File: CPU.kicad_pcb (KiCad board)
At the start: 4 copper layers, 364 x 203 mm, 212 parts, among them J1 Conn_02x36_Top_Bottom, P10 Conn_02x08_Counter_Clockwise, P2 Conn_02x13_Top_Bottom, P3 Conn_02x13_Top_Bottom, P4 Conn_02x08_Counter_Clockwise, P5 Conn_02x25_Counter_Clockwise, P6 Conn_02x25_Counter_Clockwise, P7 Conn_02x07_Counter_Clockwise, P8 Conn_02x08_Counter_Clockwise

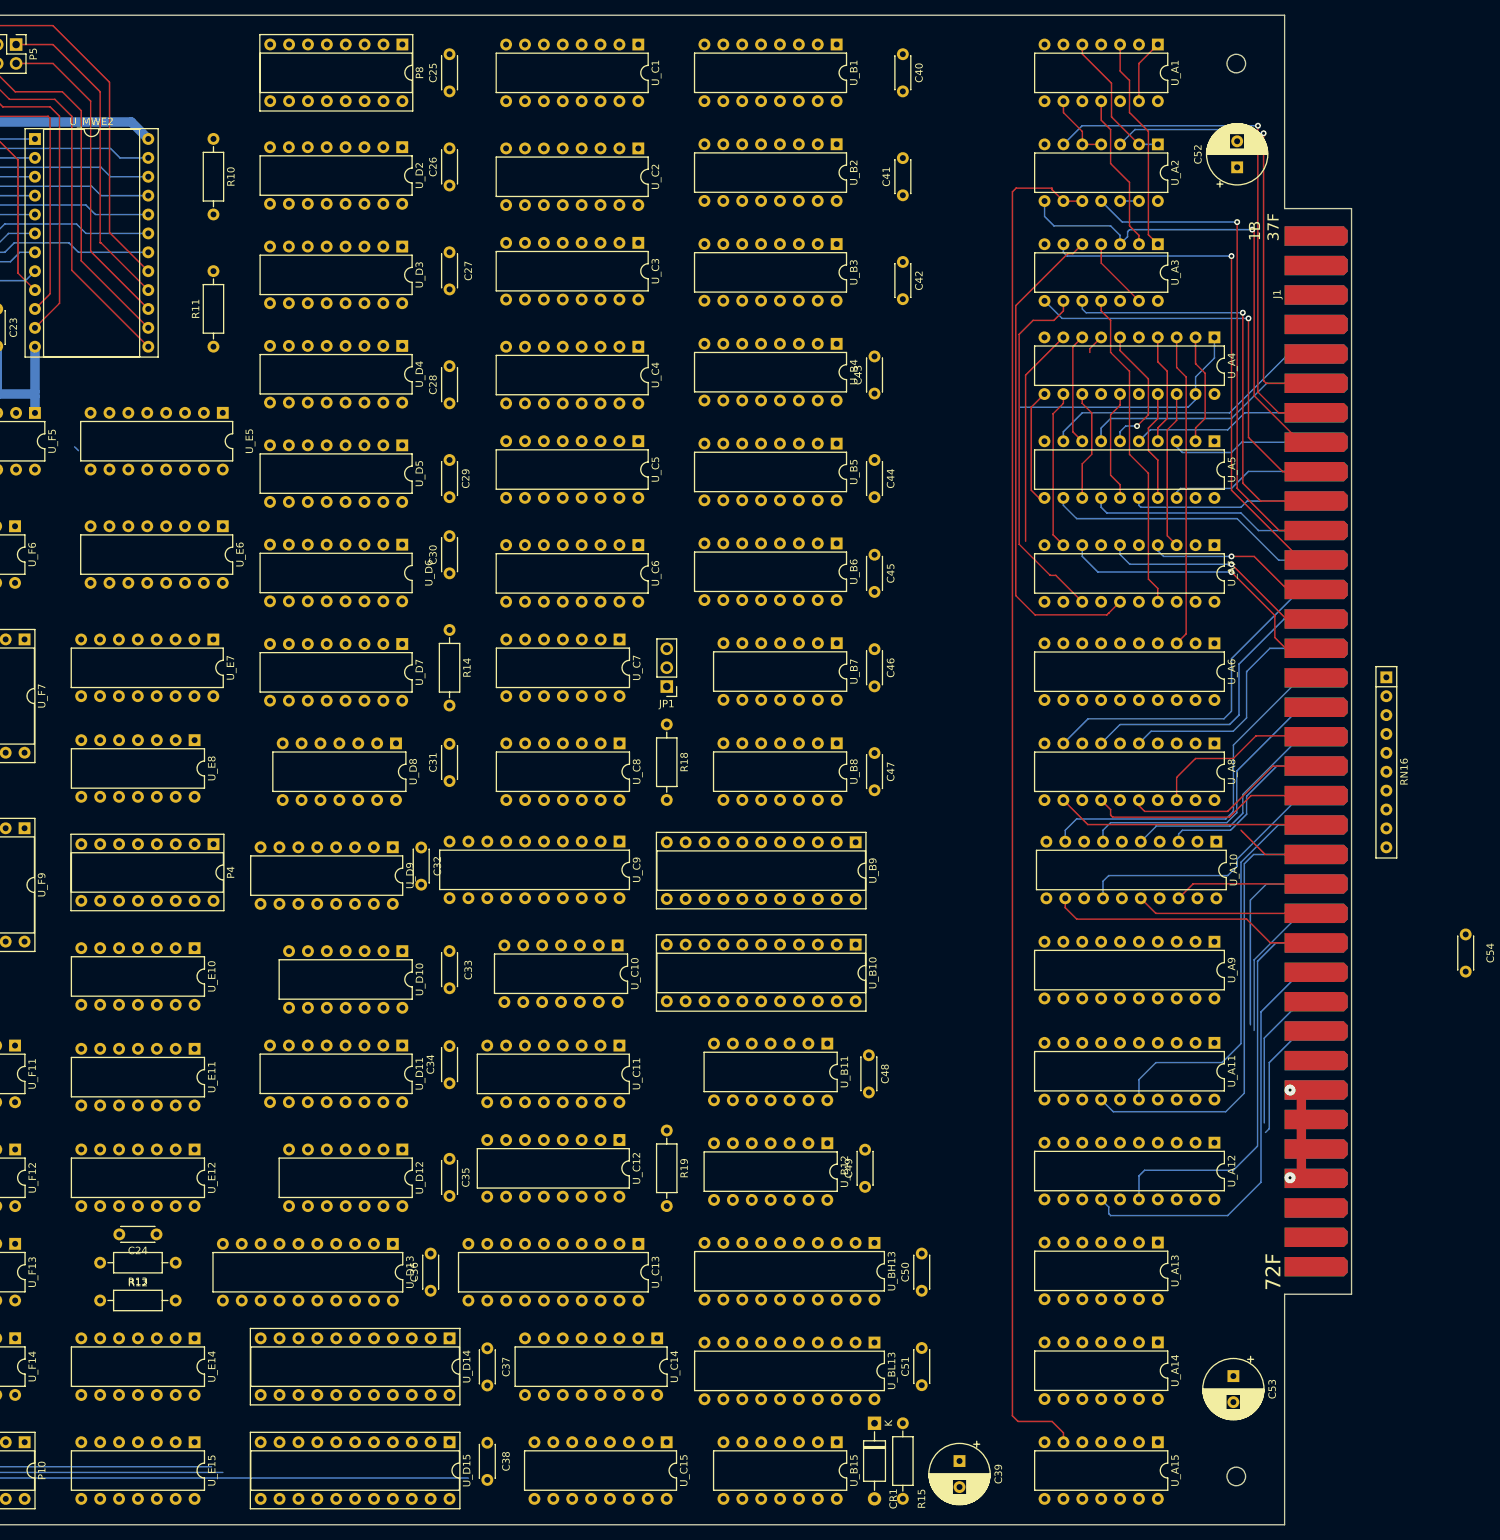
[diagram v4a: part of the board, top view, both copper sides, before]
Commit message: First row of chips successfully routed
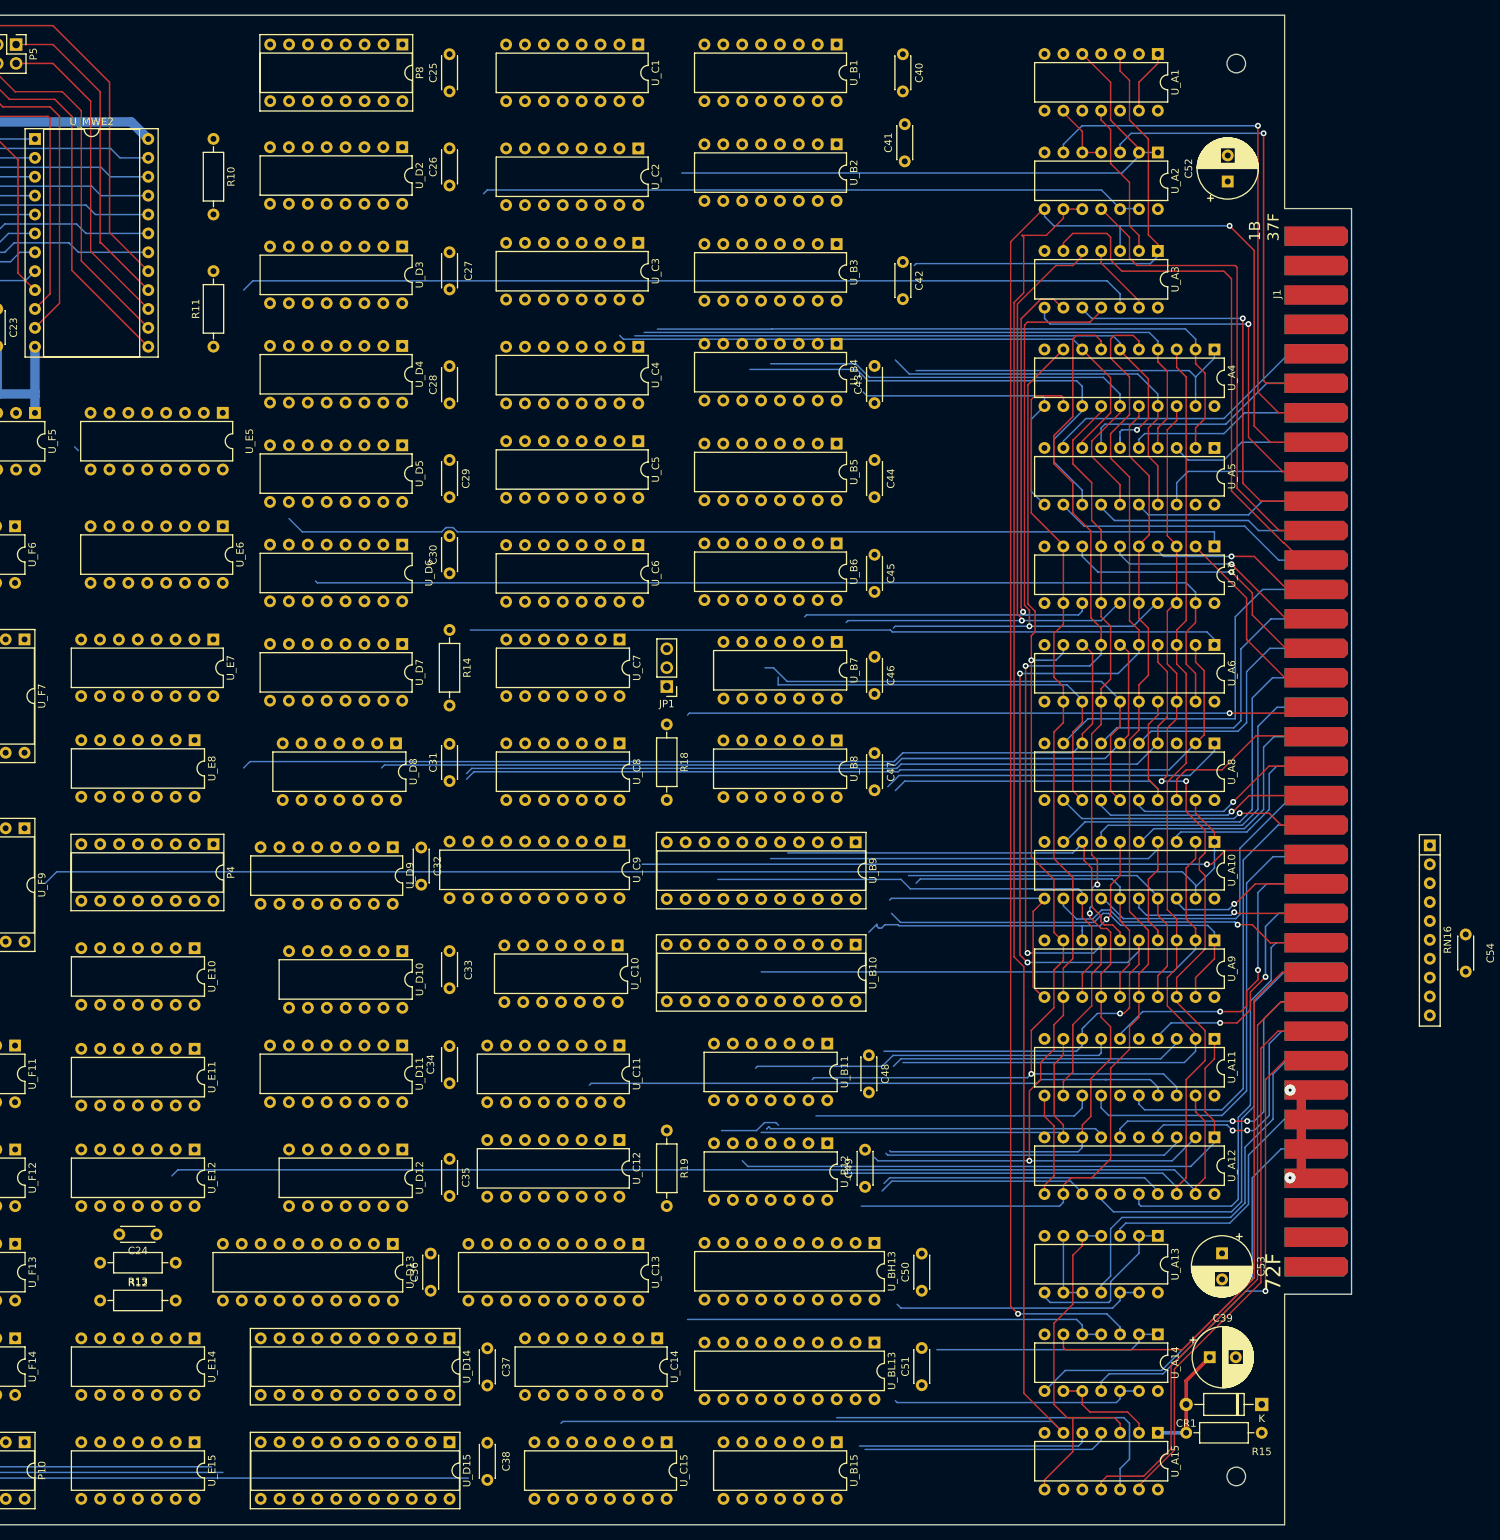
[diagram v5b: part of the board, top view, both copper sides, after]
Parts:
- moved CR1 52.1 mm to (375.9, 210.8), turned to 180 degrees
- moved R15 49.1 mm to (375.9, 214.6), turned to 180 degrees
- moved C39 36.4 mm to (368.9, 204.5), turned to 0 degrees
- moved RN16 23.3 mm to (398.5, 135.6)
- moved C53 16.6 mm to (370.6, 190.5)
- moved C41 4.57 mm to (327.9, 43.6)
- moved C52 2.29 mm to (371.3, 46.4)
- moved U_A4 1.62 mm to (369.6, 68.9)
- moved C43 1.28 mm to (323.9, 76.2)
- moved U_A1 1.27 mm to (361.9, 29.2)
- moved U_A15 1.26 mm to (362.0, 214.6)
- moved U_A2 1.09 mm to (362.0, 42.5)
- moved U_A14 1.08 mm to (362.0, 201.4)
- moved C46 1.03 mm to (323.9, 110.3)
- moved U_A3 0.91 mm to (362.0, 55.7)
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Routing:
- net /~{AddrHToSys}: track 0.00 -> 172.1 mm
- net DataP.D_{2}: track 23.9 -> 194.9 mm, vias 0 -> 3
- net /Sys.~{DRDY}: track 64.8 -> 231.7 mm, vias 1 -> 2
- net /DataWTClock: track 0.00 -> 154.8 mm
- net DataP.D_{5}: track 11.9 -> 158.3 mm
- net DataP.D_{4}: track 56.1 -> 200.2 mm, vias 0 -> 2
- net DataP.D_{7}: track 23.7 -> 161.8 mm, vias 0 -> 1
- net DataP.D_{6}: track 0.00 -> 136.2 mm, vias 0 -> 2
- net /~{AddrMToData}: track 0.00 -> 134.5 mm
- net DataP.D_{1}: track 26.8 -> 159.3 mm, vias 0 -> 2
- net DataP.D_{0}: track 29.5 -> 161.2 mm, vias 0 -> 2
- net /CPL_{3}: track 0.00 -> 128.7 mm
- net /~{DSWh_INT_OE}: track 0.00 -> 127.5 mm
- net /~{DataReady}: track 0.00 -> 120.0 mm
- net /CPL_{2}: track 0.00 -> 115.1 mm
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
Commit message: Some power lines
Proof of concept - can i really do it ?
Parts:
- moved RN16 46.5 mm to (396.7, 89.2)
- moved C52 2.60 mm to (369.6, 48.3)
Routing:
- net +5V: track 406.9 -> 633.9 mm, vias 0 -> 1
- net GND: track 788.8 -> 871.0 mm
- net Net-(J1-Pad30): track 13.4 -> 33.1 mm
- net /Sys.~{WTIN}: track 71.1 -> 62.5 mm
- net /Sys.~{RDIN}: track 59.5 -> 51.7 mm
- net /Sys.~{RA_{11}}: track 89.6 -> 93.3 mm
- net /Sys.~{INTACK}: track 62.7 -> 66.0 mm
- net /Sys.~{DRDY}: track 231.7 -> 228.5 mm
- net /Sys.Reset: track 56.1 -> 59.1 mm
- net Address.A_{14}: track 86.5 -> 88.5 mm
- net /Sys.~{CPL_{2}}: track 30.0 -> 31.8 mm
- net /Sys.~{D_{1}}: track 59.4 -> 58.0 mm
- net /Sys.~{D_{6}}: track 40.6 -> 39.4 mm
- net /Sys.~{D_{7}}: track 32.8 -> 31.6 mm
- net /Sys.~{CPL_{1}}: track 26.2 -> 27.4 mm
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
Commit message: First row of chips done
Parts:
- removed RN16: 220/330, Resistor_THT:R_Array_SIP10
- added R22: 220, Resistor_THT:R_Axial_DIN0204_L3.6mm_D1.6mm_P5.08mm_Horizontal, F.Cu at (372.1, 55.4)
- added R23: 330, Resistor_THT:R_Axial_DIN0204_L3.6mm_D1.6mm_P5.08mm_Horizontal, F.Cu at (367.0, 53.1)
- added R24: 220, Resistor_THT:R_Axial_DIN0204_L3.6mm_D1.6mm_P2.54mm_Vertical, F.Cu at (365.8, 200.2)
- added R25: 330, Resistor_THT:R_Axial_DIN0204_L3.6mm_D1.6mm_P2.54mm_Vertical, F.Cu at (373.4, 200.2)
- added R26: 220, Resistor_THT:R_Axial_DIN0204_L3.6mm_D1.6mm_P2.54mm_Vertical, F.Cu at (365.8, 197.9)
- added R27: 330, Resistor_THT:R_Axial_DIN0204_L3.6mm_D1.6mm_P2.54mm_Vertical, F.Cu at (373.4, 197.9)
- added RN20: 220, Resistor_THT:R_Array_SIP5, F.Cu at (374.6, 120.2)
- added RN21: 330, Resistor_THT:R_Array_SIP5, F.Cu at (374.6, 96.0)
- moved C54 76.0 mm to (327.4, 150.4)
- moved C44 17.5 mm to (340.9, 87.8), turned to 90 degrees
- moved C43 17.0 mm to (340.9, 75.1)
- moved C41 14.0 mm to (340.9, 49.0)
- moved C42 14.0 mm to (340.9, 61.7), turned to 90 degrees
- moved C40 13.3 mm to (340.9, 30.8)
- moved C39 1.27 mm to (368.9, 205.7)
- moved CR1 1.27 mm to (375.9, 212.1)
- moved R15 1.27 mm to (375.9, 215.9)
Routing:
- net GND: track 871.0 -> 993.1 mm
- net +5V: track 633.9 -> 690.7 mm
- net /~{Reset_{2}}: track 8.68 -> 38.3 mm
- net /Sys.~{INR1}: track 22.4 -> 45.0 mm, vias 1 -> 0
- net /Sys.~{INR2}: track 29.2 -> 48.0 mm, vias 1 -> 0
- net /Sys.~{INR3}: track 37.8 -> 47.8 mm, vias 1 -> 0
- net /Sys.~{INR0}: track 25.0 -> 32.7 mm
- net Address.A_{1}: track 64.7 -> 71.2 mm
- net /Sys.~{RA_{15}}: track 83.0 -> 88.5 mm
- net Net-(U_A10-Pad6): track 46.6 -> 41.7 mm
- net /Sys.~{PTR7_oc}: track 76.1 -> 79.3 mm
- net /Sys.~{INTREQ}: track 81.2 -> 84.2 mm
- net /Sys.~{MemFault}: track 72.5 -> 75.5 mm
- net /Sys.~{APRE}: track 63.0 -> 60.2 mm
- net /Sys.~{RDIN}: track 51.7 -> 49.4 mm
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
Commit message: Rounting WIP
Second row almost done.
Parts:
- R18: footprint Resistor_THT:R_Axial_DIN0207_L6.3mm_D2.5mm_P10.16mm_Horizontal -> Resistor_THT:R_Axial_DIN0207_L6.3mm_D2.5mm_P7.62mm_Horizontal
- R19: footprint Resistor_THT:R_Axial_DIN0207_L6.3mm_D2.5mm_P10.16mm_Horizontal -> Resistor_THT:R_Axial_DIN0204_L3.6mm_D1.6mm_P7.62mm_Horizontal
- moved C54 71.3 mm to (340.9, 220.4), turned to 90 degrees
- moved R19 39.3 mm to (334.3, 182.5), turned to 90 degrees
- moved R18 20.9 mm to (314.2, 129.5), turned to 90 degrees
- moved U_B10 19.1 mm to (340.4, 148.4)
- moved U_B9 19.1 mm to (340.4, 135.2)
- moved C49 18.3 mm to (340.9, 181.1)
- moved JP1 18.2 mm to (313.7, 110.2), turned to 0 degrees
- moved C48 17.9 mm to (340.9, 162.1)
- moved C45 16.0 mm to (339.1, 101.6), turned to 90 degrees
- moved C47 15.2 mm to (339.1, 122.7)
- moved C46 15.2 mm to (339.1, 110.3)
- moved U_B8 14.0 mm to (332.7, 121.9)
- moved U_B7 14.0 mm to (332.7, 108.7)
- moved U_B1 14.0 mm to (332.7, 29.2)
- moved U_BL13 14.0 mm to (337.8, 201.4)
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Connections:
- U_B11 pad 11: /PTR.Q_{6} -> /PTR.Q_{4}
- U_B11 pad 9: /PTR.Q_{4} -> /PTR.Q_{6}
- U_B2 pad 3: /B2_P0 -> Net-(U_B2-Pad3)
- U_B2 pad 4: /B2_P1 -> Net-(U_B2-Pad4)
- U_B2 pad 5: /B2_P2 -> Net-(U_B2-Pad5)
- U_B2 pad 6: /B2_P3 -> Net-(U_B2-Pad6)
- U_B3 pad 10: Res.D_{1} -> Res.D_{2}
- U_B3 pad 11: Address.A_{1} -> Address.A_{2}
- U_B3 pad 12: /B2_P0 -> Net-(U_B2-Pad4)
- U_B3 pad 13: Res.D_{0} -> Res.D_{1}
- U_B3 pad 14: Address.A_{0} -> Address.A_{1}
- U_B3 pad 2: Address.A_{3} -> Address.A_{0}
- U_B3 pad 3: Res.D_{3} -> Res.D_{0}
- U_B3 pad 4: /B2_P3 -> Net-(U_B2-Pad3)
- U_B3 pad 5: Address.A_{2} -> Address.A_{3}
- U_B3 pad 6: Res.D_{2} -> Res.D_{3}
- U_B3 pad 7: /B2_P2 -> Net-(U_B2-Pad6)
- U_B3 pad 9: /B2_P1 -> Net-(U_B2-Pad5)
- U_B4 pad 10: Res.D_{1} -> Res.D_{3}
- U_B4 pad 11: Address.A_{9} -> Address.A_{11}
- U_B4 pad 13: Res.D_{0} -> Res.D_{1}
- U_B4 pad 14: Address.A_{8} -> Address.A_{9}
- U_B4 pad 2: Address.A_{11} -> Address.A_{8}
- U_B4 pad 3: Res.D_{3} -> Res.D_{0}
- U_B4 pad 4: Net-(U_B4-Pad4) -> Net-(U_B5-Pad3)
- U_B4 pad 9: Net-(U_B4-Pad9) -> Net-(U_B5-Pad6)
- U_B5 pad 3: Net-(U_B4-Pad12) -> Net-(U_B5-Pad3)
- U_B5 pad 4: Net-(U_B4-Pad9) -> Net-(U_B4-Pad12)
- U_B5 pad 6: Net-(U_B4-Pad4) -> Net-(U_B5-Pad6)
- U_C2 pad 3: /C2_P0 -> Net-(U_C2-Pad3)
- U_C2 pad 4: /C2_P1 -> Net-(U_C2-Pad4)
- U_C2 pad 5: /C2_P2 -> Net-(U_C2-Pad5)
- U_C2 pad 6: /C2_P3 -> Net-(U_C2-Pad6)
- U_C3 pad 10: Res.D_{5} -> Res.D_{6}
- U_C3 pad 11: Address.A_{5} -> Address.A_{6}
- U_C3 pad 12: /C2_P0 -> Net-(U_C2-Pad4)
- U_C3 pad 13: Res.D_{4} -> Res.D_{5}
- U_C3 pad 14: Address.A_{4} -> Address.A_{5}
- U_C3 pad 2: Address.A_{7} -> Address.A_{4}
- U_C3 pad 3: Res.D_{7} -> Res.D_{4}
- U_C3 pad 4: /C2_P3 -> Net-(U_C2-Pad3)
- U_C3 pad 5: Address.A_{6} -> Address.A_{7}
- U_C3 pad 6: Res.D_{6} -> Res.D_{7}
- U_C3 pad 7: /C2_P2 -> Net-(U_C2-Pad6)
- U_C3 pad 9: /C2_P1 -> Net-(U_C2-Pad5)
- U_C4 pad 10: Res.D_{5} -> Res.D_{7}
- U_C4 pad 11: Address.A_{13} -> Address.A_{15}
- U_C4 pad 13: Res.D_{4} -> Res.D_{5}
- U_C4 pad 14: Address.A_{12} -> Address.A_{13}
- U_C4 pad 2: Address.A_{15} -> Address.A_{12}
- U_C4 pad 3: Res.D_{7} -> Res.D_{4}
- U_C4 pad 9: Net-(U_C4-Pad9) -> Net-(U_C5-Pad6)
- U_C5 pad 3: Net-(U_C4-Pad12) -> Net-(U_C4-Pad4)
- U_C5 pad 4: Net-(U_C4-Pad9) -> Net-(U_C4-Pad12)
- U_C5 pad 6: Net-(U_C4-Pad4) -> Net-(U_C5-Pad6)
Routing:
- net /~{PTRAM_WE}: track 0.00 -> 225.4 mm
- net /~{DataWTCycle}: track 0.00 -> 178.1 mm, vias 0 -> 1
- net Net-(U_B1-Pad2): track 0.00 -> 156.1 mm
- net /~{DataRDCycle}: track 0.00 -> 152.2 mm, vias 0 -> 1
- net Res.D_{0}: track 0.00 -> 148.8 mm, vias 0 -> 2
- net Res.D_{3}: track 0.00 -> 147.8 mm, vias 0 -> 2
- net Res.D_{1}: track 0.00 -> 144.9 mm, vias 0 -> 1
- net /PTR.Q_{7}: track 57.2 -> 196.1 mm, vias 0 -> 3
- net Address.A_{11}: track 52.3 -> 186.9 mm, vias 0 -> 2
- net /ParitySelect: track 34.2 -> 165.5 mm
- net Address.A_{8}: track 0.00 -> 126.5 mm, vias 0 -> 1
- net /DataRDCycle: track 81.8 -> 204.9 mm, vias 0 -> 1
- net Net-(U_B10-Pad18): track 0.00 -> 120.8 mm
- net /MemAddr_LD_SWAP: track 0.00 -> 118.2 mm, vias 0 -> 1
- net /Addr U/D: track 0.00 -> 114.4 mm
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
